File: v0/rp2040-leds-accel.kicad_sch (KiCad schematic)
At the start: 12 parts, among them J1 USB_C_Receptacle_USB2.0_16P, U1 AMS1117-3.3, U2 AMS1117-5

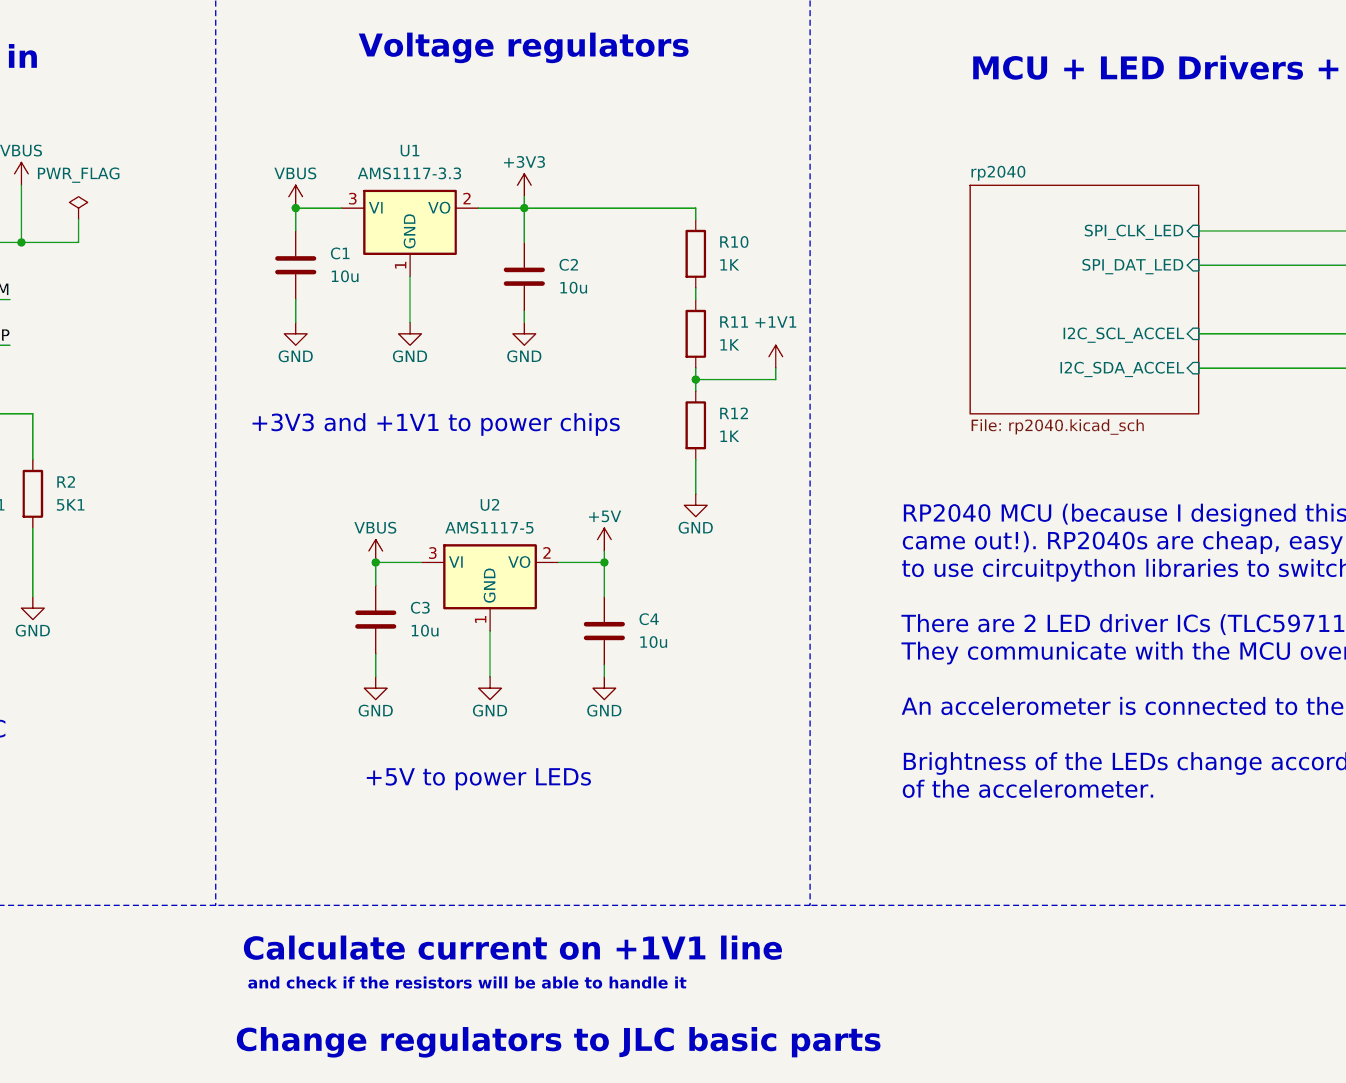
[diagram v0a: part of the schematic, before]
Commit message: Picked new LED driver TLC59116, conected over I2C (instead of the previous one that used SPI), increased number of LEDs from 24 to 32.
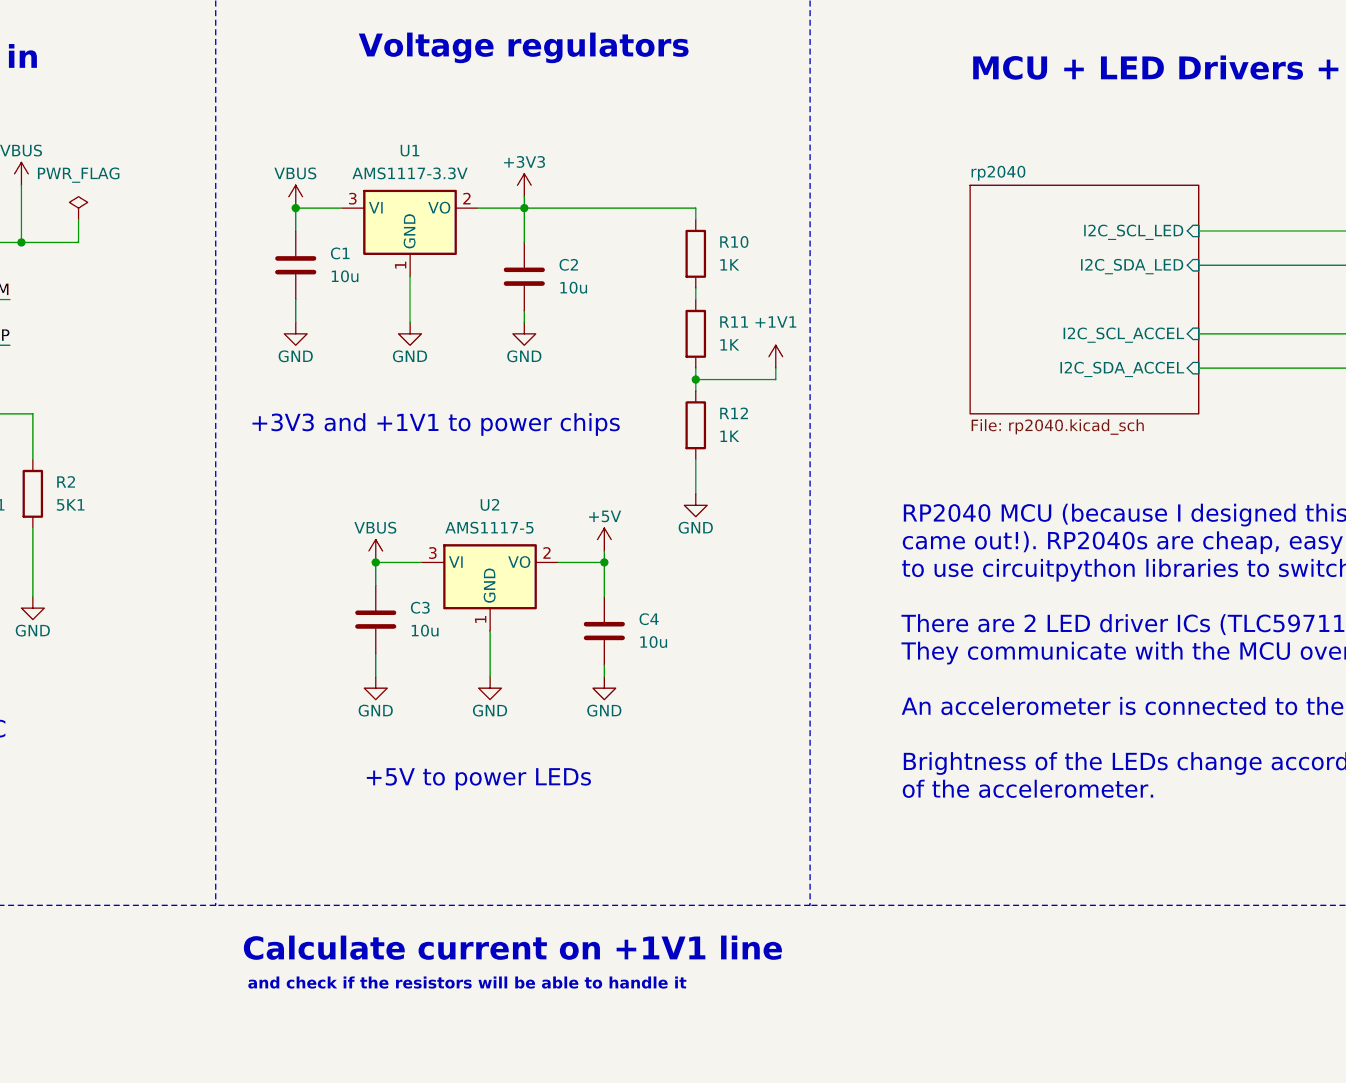
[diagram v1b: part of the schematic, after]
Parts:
- removed U1: AMS1117-3.3, Package_TO_SOT_SMD:SOT-223-3_TabPin2, symbol suchi_chips:AMS1117-3.3
- added U1: AMS1117-3.3V, Package_TO_SOT_SMD:SOT-223-3_TabPin2, symbol suchi_chips:AMS1117-3.3V
- U2: MFG Advanced Monolithic Systems -> Advanced Monolithic Systems; MPN AMS1117-3.3V -> AMS1117-5.0
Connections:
- net +3V3: now also U1.2 (VO)
- net GND: now also U1.1 (GND)
- net VBUS: now also U1.3 (VI)
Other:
- sheet rp2040 ports: added I2C_SCL_LED, I2C_SDA_LED; removed SPI_CLK_LED, SPI_DAT_LED
- note removed: "Change regulators to JLC basic parts"
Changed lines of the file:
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@@
-		)
-	)
-	(text "Change regulators to JLC basic parts"
-		(exclude_from_sim no)
-		(at 139.7 167.64 0)
-		(effects
-			(font
-				(size 2.54 2.54)
-				(bold yes)
-				(color 255 0 0 1)
-			)
 		)
 	)
@@
 			)
 		)
-		(property "Description" "1A Low Dropout regulator, positive, 5V fixed output, SOT-223"
+		(property "Description" "68dB@(120Hz) 1A Fixed 5V Positive electrode 12V SOT-223 Voltage Regulators - Linear, Low Drop Out (LDO) Regulators ROHS"
 			(at 132.08 116.84 0)
 			(effects
@@
 			)
 		)
-		(property "MFG" "Advanced Monolithic Systems"
+		(property "MFG" "Advanced Monolithic Systems "
 			(at 132.08 116.84 0)
 			(effects
@@
 			)
 		)
-		(property "MPN" "AMS1117-3.3V"
+		(property "MPN" "AMS1117-5.0 "
 			(at 132.08 116.84 0)
 			(effects
@@
 	)
 	(symbol
+		(lib_id "suchi_chips:AMS1117-3.3V")
+		(at 123.19 77.47 0)
+		(unit 1)
+		(exclude_from_sim no)
+		(in_bom yes)
+		(on_board yes)
+		(dnp no)
+		(fields_autoplaced yes)
+		(property "Reference" "U1"
+			(at 123.19 68.58 0)
+			(effects
+				(font
+					(size 1.27 1.27)
+				)
+			)
+		)
+		(property "Value" "AMS1117-3.3V"
+			(at 123.19 71.12 0)
+			(effects
+				(font
+					(size 1.27 1.27)
+				)
+			)
+		)
+		(property "Footprint" "Package_TO_SOT_SMD:SOT-223-3_TabPin2"
+			(at 123.19 77.47 0)
+			(effects
+				(font
+					(size 1.27 1.27)
+				)
+				(hide yes)
+			)
+		)
+		(property "Datasheet" ""
+			(at 123.19 77.47 0)
+			(effects
+				(font
+					(size 1.27 1.27)
+				)
+				(hide yes)
+			)
+		)
+		(property "Description" "72dB@(120Hz) 1A Fixed 3.3V Positive electrode SOT-223 Voltage Regulators - Linear, Low Drop Out (LDO) Regulators ROHS"
+			(at 123.19 77.47 0)
+			(effects
+				(font
+					(size 1.27 1.27)
+				)
+				(hide yes)
+			)
+		)
+		(property "MFG" "Advanced Monolithic Systems "
+			(at 123.19 77.47 0)
+			(effects
+				(font
+					(size 1.27 1.27)
+				)
+				(hide yes)
+			)
+		)
+		(property "MPN" "AMS1117-3.3 "
+			(at 123.19 77.47 0)
+			(effects
+				(font
+					(size 1.27 1.27)
+				)
+				(hide yes)
+			)
+		)
+		(property "JLC" "C6186"
+			(at 123.19 77.47 0)
+			(effects
+				(font
+					(size 1.27 1.27)
+				)
+				(hide yes)
+			)
+		)
+		(pin "3"
+		)
+		(pin "2"
+		)
+		(pin "1"
+		)
+		(instances
+			(project ""
+				(path "/9724e854-62b2-4906-81a1-7cf114a24039"
+					(reference "U1")
+					(unit 1)
+				)
+			)
+		)
+	)
+	(symbol
 		(lib_id "power:GND")
 		(at 135.89 87.63 0)
@@
 				(path "/9724e854-62b2-4906-81a1-7cf114a24039"
 					(reference "R1")
-					(unit 1)
-				)
-			)
-		)
-	)
-	(symbol
-		(lib_id "suchi_chips:AMS1117-3.3")
-		(at 123.19 77.47 0)
-		(unit 1)
-		(exclude_from_sim no)
-		(in_bom yes)
-		(on_board yes)
-		(dnp no)
-		(fields_autoplaced yes)
-		(property "Reference" "U1"
-			(at 123.19 68.58 0)
-			(effects
-				(font
-					(size 1.27 1.27)
-				)
-			)
-		)
-		(property "Value" "AMS1117-3.3"
-			(at 123.19 71.12 0)
-			(effects
-				(font
-					(size 1.27 1.27)
-				)
-			)
-		)
-		(property "Footprint" "Package_TO_SOT_SMD:SOT-223-3_TabPin2"
-			(at 123.19 77.47 0)
-			(effects
-				(font
-					(size 1.27 1.27)
-				)
-				(hide yes)
-			)
-		)
-		(property "Datasheet" "http://www.advanced-monolithic.com/pdf/ds1117.pdf"
-			(at 123.19 77.47 0)
-			(effects
-				(font
-					(size 1.27 1.27)
-				)
-				(hide yes)
-			)
-		)
-		(property "Description" "1A Low Dropout regulator, positive, 3.3V fixed output, SOT-223"
-			(at 123.19 77.47 0)
-			(effects
-				(font
-					(size 1.27 1.27)
-				)
-				(hide yes)
-			)
-		)
-		(property "JLC" "C5120765"
-			(at 123.19 77.47 0)
-			(effects
-				(font
-					(size 1.27 1.27)
-				)
-				(hide yes)
-			)
-		)
-		(property "MFG" "MSKSEMI"
-			(at 123.19 77.47 0)
-			(effects
-				(font
-					(size 1.27 1.27)
-				)
-				(hide yes)
-			)
-		)
-		(property "MPN" "AMS1117-3.3V"
-			(at 123.19 77.47 0)
-			(effects
-				(font
-					(size 1.27 1.27)
-				)
-				(hide yes)
-			)
-		)
-		(pin "2"
-		)
-		(pin "3"
-		)
-		(pin "1"
-		)
-		(instances
-			(project "rp2040-leds-accel"
-				(path "/9724e854-62b2-4906-81a1-7cf114a24039"
-					(reference "U1")
 					(unit 1)
 				)
@@
 			)
 		)
-		(pin "SPI_CLK_LED" input
+		(pin "I2C_SCL_LED" input
 			(at 210.82 77.47 0)
 			(effects
@@
 			)
 		)
-		(pin "SPI_DAT_LED" input
+		(pin "I2C_SDA_LED" input
 			(at 210.82 81.28 0)
 			(effects
